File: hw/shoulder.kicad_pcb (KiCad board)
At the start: 2 copper layers, 60 x 40 mm, 27 parts, among them J1 IDC_02X07, U1 OSRB38C9BA, U2 OSRB38C9BA, U3 OSRB38C9BA, U4 OSRB38C9BA, U5 OSRB38C9BA

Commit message: updated pcb
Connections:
- LS1 pad 3: Net-(LS1-Pad3) -> GND
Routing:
- added copper zone on B.Cu, net GND
- added copper zone on F.Cu, net GND
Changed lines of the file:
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@@
     (zones 0)
     (modules 27)
-    (nets 21)
+    (nets 20)
   )
   (page A4)
@@
   (setup
     (last_trace_width 0.25)
+    (user_trace_width 0.5)
+    (user_trace_width 1)
     (trace_clearance 0.2)
     (zone_clearance 0.508)
@@
     (mod_text_size 1 1)
     (mod_text_width 0.15)
-    (pad_size 1.524 1.524)
-    (pad_drill 0.762)
+    (pad_size 6 3)
+    (pad_drill 2)
     (pad_to_mask_clearance 0.2)
     (aux_axis_origin 0 0)
@@
   (net 18 /SP+)
   (net 19 /SP-)
-  (net 20 "Net-(LS1-Pad3)")
   (net_class Default "Toto je výchozí třída sítě."
     (clearance 0.2)
@@
     (add_net "Net-(D2-Pad2)")
     (add_net "Net-(D2-Pad3)")
-    (add_net "Net-(LS1-Pad3)")
   )
   (module KLIB_Audio:REP-ABS-224-RC (layer F.Cu)
@@
     (fp_line (start 10 -20) (end 10 -19.75) (layer F.SilkS) (width 0.15))
     (fp_line (start -10 -20) (end -10 -19.75) (layer F.SilkS) (width 0.15))
-    (pad 1 smd rect (at -3 21 90) (size 4 3) (layers B.Cu B.Paste B.Mask)
+    (pad 1 smd rect (at 24 13 90) (size 1.5 3) (layers B.Cu B.Paste B.Mask)
       (net 18 /SP+))
-    (pad 2 smd rect (at 3 21 90) (size 4 3) (layers B.Cu B.Paste B.Mask)
+    (pad 2 smd oval (at 24 18 90) (size 1.5 3) (layers B.Cu B.Paste B.Mask)
       (net 19 /SP-))
     (pad 3 thru_hole oval (at 8 18 90) (size 6 3) (drill 2 (offset 1 0)) (layers *.Cu *.Mask)
-      (net 20 "Net-(LS1-Pad3)"))
+      (net 17 GND) (zone_connect 2))
     (pad 3 thru_hole oval (at 8 -18 90) (size 6 3) (drill 2 (offset 1 0)) (layers *.Cu *.Mask)
-      (net 20 "Net-(LS1-Pad3)"))
+      (net 17 GND) (zone_connect 2))
     (pad 3 thru_hole oval (at -8 -18 90) (size 6 3) (drill 2 (offset -1 0)) (layers *.Cu *.Mask)
-      (net 20 "Net-(LS1-Pad3)"))
+      (net 17 GND) (zone_connect 2))
     (pad 3 thru_hole oval (at -8 18 90) (size 6 3) (drill 2 (offset -1 0)) (layers *.Cu *.Mask)
-      (net 20 "Net-(LS1-Pad3)"))
+      (net 17 GND) (zone_connect 2))
     (pad 3 thru_hole oval (at 11 -18 90) (size 6 3) (drill 2 (offset -1 0)) (layers *.Cu *.Mask)
-      (net 20 "Net-(LS1-Pad3)"))
+      (net 17 GND) (zone_connect 2))
     (pad 3 thru_hole oval (at -11 -18 90) (size 6 3) (drill 2 (offset 1 0)) (layers *.Cu *.Mask)
-      (net 20 "Net-(LS1-Pad3)"))
+      (net 17 GND) (zone_connect 2))
     (pad 3 thru_hole oval (at 11 18 90) (size 6 3) (drill 2 (offset -1 0)) (layers *.Cu *.Mask)
-      (net 20 "Net-(LS1-Pad3)"))
+      (net 17 GND) (zone_connect 2))
     (pad 3 thru_hole oval (at -11 18 90) (size 6 3) (drill 2 (offset 1 0)) (layers *.Cu *.Mask)
-      (net 20 "Net-(LS1-Pad3)"))
+      (net 17 GND) (zone_connect 2))
     (model "$(KIPRJMOD)/project.3dshapes/ABS-224-RC.wrl"
       (at (xyz 0 0 0))
@@
   (gr_line (start 185 120) (end 185 80) (layer Edge.Cuts) (width 0.15))
   (gr_line (start 125 120) (end 185 120) (layer Edge.Cuts) (width 0.15))
+  (zone (net 17) (net_name GND) (layer F.Cu) (hatch edge 0.508)
+    (connect_pads (clearance 0.508))
+    (min_thickness 0.254)
+    (fill yes (arc_segments 16) (thermal_gap 0.508) (thermal_bridge_width 0.508))
+    (polygon
+      (pts
+        (xy 125 120) (xy 185 120) (xy 185 80) (xy 125 80)
+      )
+    )
+  )
+  (zone (net 17) (net_name GND) (layer B.Cu) (hatch edge 0.508)
+    (connect_pads (clearance 0.508))
+    (min_thickness 0.254)
+    (fill yes (arc_segments 16) (thermal_gap 0.508) (thermal_bridge_width 0.508))
+    (polygon
+      (pts
+        (xy 125 80) (xy 185 80) (xy 185 120) (xy 125 120)
+      )
+    )
+  )
 )

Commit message: updated pcb
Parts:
- moved C1 0.50 mm to (136.5, 83.5)
- moved C2 0.50 mm to (173.5, 83.5)
- moved R1 0.50 mm to (136.5, 86.2)
- moved R10 0.50 mm to (173.5, 90.2)
- moved R11 0.50 mm to (173.5, 88.2)
- moved R2 0.50 mm to (173.5, 86.2)
- moved R6 0.50 mm to (136.5, 88.2)
- moved R7 0.50 mm to (136.5, 90.2)
- moved R8 0.50 mm to (136.5, 92.2)
- moved R9 0.50 mm to (173.5, 92.2)
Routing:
- net +5V: track 0.00 -> 121.1 mm, vias 0 -> 8
- net /IR_RX: track 0.00 -> 67.0 mm
- net /SP-: track 0.00 -> 14.4 mm
- net Net-(C4-Pad1): track 0.00 -> 11.7 mm
- net Net-(C3-Pad1): track 0.00 -> 8.34 mm
- net /SP+: track 0.00 -> 6.00 mm
- net Net-(C5-Pad1): track 0.00 -> 5.78 mm
- net Net-(D2-Pad3): track 0.00 -> 4.03 mm
- net Net-(D1-Pad1): track 0.00 -> 4.03 mm
- net Net-(D2-Pad2): track 0.00 -> 3.90 mm
- net Net-(D1-Pad2): track 0.00 -> 3.90 mm
- net Net-(D2-Pad1): track 0.00 -> 3.78 mm
- net Net-(D1-Pad3): track 0.00 -> 3.78 mm

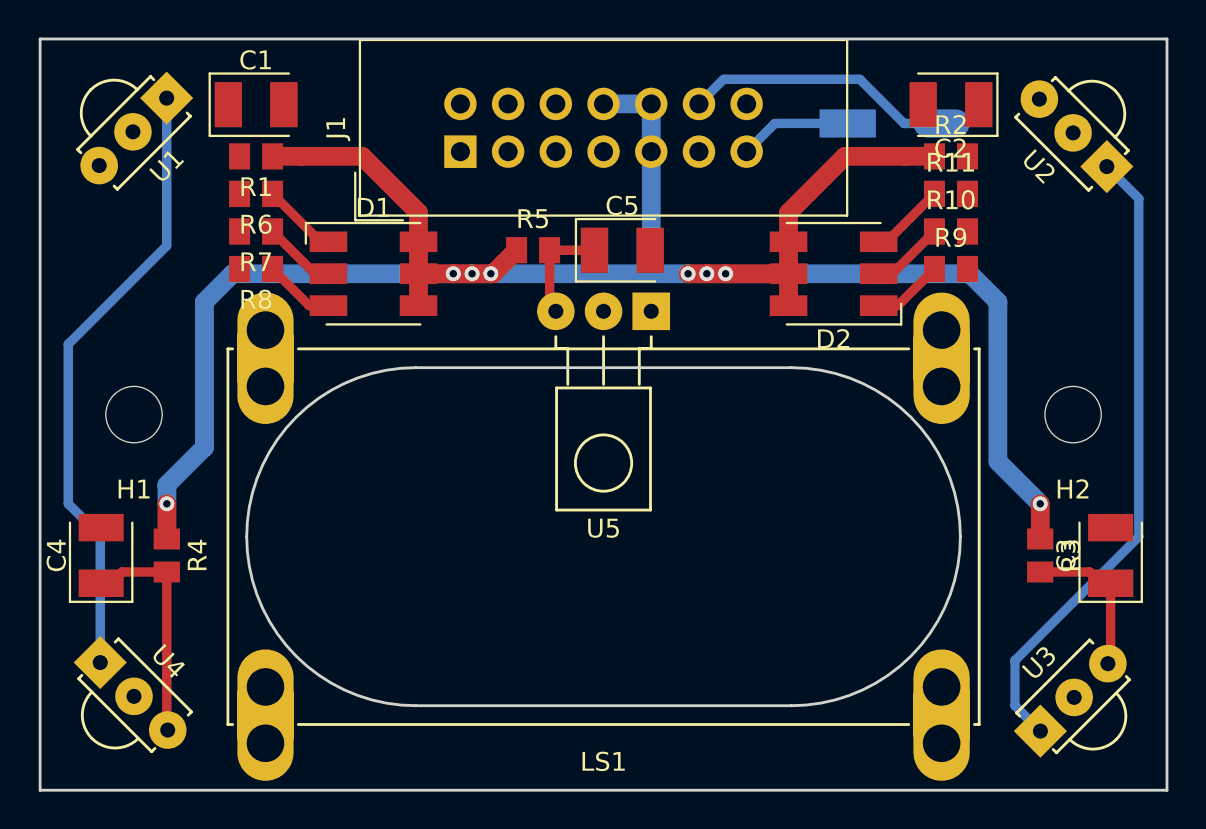
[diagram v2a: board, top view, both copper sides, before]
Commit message: updated pcb all nets conected
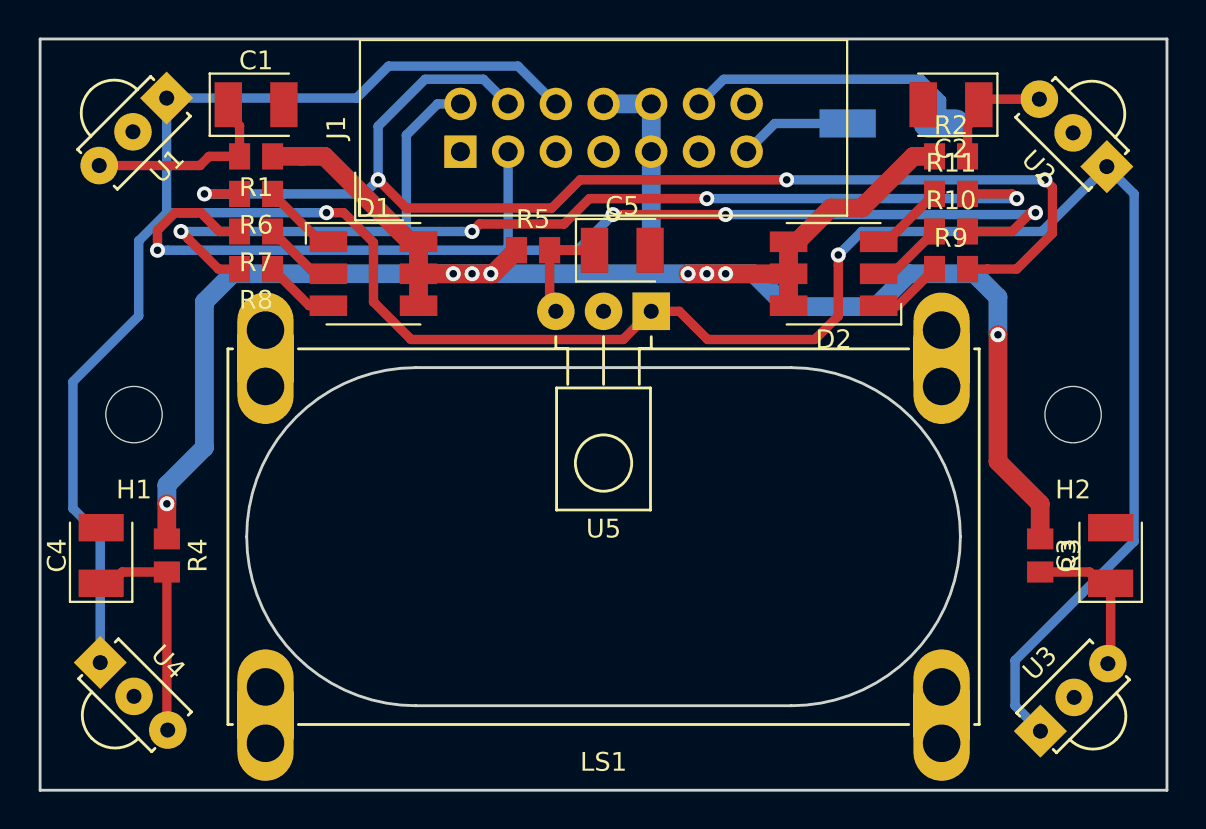
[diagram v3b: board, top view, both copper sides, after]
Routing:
- net /IR_RX: track 67.0 -> 150.5 mm, vias 0 -> 2
- net /PWM_B: track 0.00 -> 67.8 mm, vias 0 -> 4
- net /PWM_G: track 0.00 -> 63.2 mm, vias 0 -> 4
- net /PWM_R: track 0.00 -> 60.6 mm, vias 0 -> 4
- net Net-(C1-Pad1): track 0.00 -> 10.7 mm
- net Net-(C2-Pad1): track 0.00 -> 6.36 mm
- net /SP-: track 14.4 -> 15.2 mm

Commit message: updated pcb
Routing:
- net /IR_RX: track 150.5 -> 156.3 mm, vias 2 -> 3
- net +5V: track 120.9 -> 119.4 mm
- net /PWM_B: track 67.8 -> 66.8 mm
- net /PWM_R: track 60.6 -> 59.9 mm

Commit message: updated pcb
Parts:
- added G***: LOGO, KLIB_Logo:wykys_small_skill, F.Cu at (130.5, 94.8)
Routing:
- net GND: vias 0 -> 6
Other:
- board text added: "SHOULDER V3"

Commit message: updated pcb
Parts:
- added REF**: Fiducial_Pad_1mm_Outer_2mm, KLIB_Mechanical:Fiducial_Pad_1mm_Outer_2mm, F.Cu at (180.0, 93.0)
- added REF**: Fiducial_Pad_1mm_Outer_2mm, KLIB_Mechanical:Fiducial_Pad_1mm_Outer_2mm, F.Cu at (128.0, 91.0)
- added REF**: Fiducial_Pad_1mm_Outer_2mm, KLIB_Mechanical:Fiducial_Pad_1mm_Outer_2mm, F.Cu at (177.0, 112.0)
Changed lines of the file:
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@@
     (tracks 217)
     (zones 0)
-    (modules 28)
+    (modules 31)
     (nets 20)
   )
@@
     (fp_line (start 9 10) (end 9 -10) (layer F.Fab) (width 0.15))
     (fp_arc (start 0 -10) (end 0 -19) (angle 90) (layer F.Fab) (width 0.15))
-    (fp_text user %R (at 2 0 180) (layer F.Fab)
+    (fp_text user %R (at -1.5 0 180) (layer F.Fab)
       (effects (font (size 1 1) (thickness 0.15)))
     )
@@
       (xy 0.058362 -0.86999)) (layer F.SilkS) (width 0.01))
   )
+  (module KLIB_Mechanical:Fiducial_Pad_1mm_Outer_2mm (layer F.Cu)
+    (at 180 93)
+    (descr "Circular Fiducial, 0.5mm bare copper top; 1mm keepout (Level C)")
+    (tags marker)
+    (attr virtual)
+    (fp_text reference REF** (at 0 -1.5) (layer F.SilkS) hide
+      (effects (font (size 1 1) (thickness 0.15)))
+    )
+    (fp_text value Fiducial_Pad_1mm_Outer_2mm (at 0 1.5) (layer F.Fab)
+      (effects (font (size 1 1) (thickness 0.15)))
+    )
+    (fp_circle (center 0 0) (end 0.75 0) (layer F.CrtYd) (width 0.05))
+    (fp_text user %R (at 0 0) (layer F.Fab)
+      (effects (font (size 0.2 0.2) (thickness 0.04)))
+    )
+    (fp_circle (center 0 0) (end 0.5 0) (layer F.Fab) (width 0.1))
+    (pad ~ smd circle (at 0 0) (size 1 1) (layers F.Cu F.Mask)
+      (solder_mask_margin 0.5) (clearance 0.5))
+  )
+  (module KLIB_Mechanical:Fiducial_Pad_1mm_Outer_2mm (layer F.Cu)
+    (at 128 91)
+    (descr "Circular Fiducial, 0.5mm bare copper top; 1mm keepout (Level C)")
+    (tags marker)
+    (attr virtual)
+    (fp_text reference REF** (at 0 -1.5) (layer F.SilkS) hide
+      (effects (font (size 1 1) (thickness 0.15)))
+    )
+    (fp_text value Fiducial_Pad_1mm_Outer_2mm (at 0 1.5) (layer F.Fab)
+      (effects (font (size 1 1) (thickness 0.15)))
+    )
+    (fp_circle (center 0 0) (end 0.75 0) (layer F.CrtYd) (width 0.05))
+    (fp_text user %R (at 0 0) (layer F.Fab)
+      (effects (font (size 0.2 0.2) (thickness 0.04)))
+    )
+    (fp_circle (center 0 0) (end 0.5 0) (layer F.Fab) (width 0.1))
+    (pad ~ smd circle (at 0 0) (size 1 1) (layers F.Cu F.Mask)
+      (solder_mask_margin 0.5) (clearance 0.5))
+  )
+  (module KLIB_Mechanical:Fiducial_Pad_1mm_Outer_2mm (layer F.Cu)
+    (at 177 112)
+    (descr "Circular Fiducial, 0.5mm bare copper top; 1mm keepout (Level C)")
+    (tags marker)
+    (attr virtual)
+    (fp_text reference REF** (at 0 -1.5) (layer F.SilkS) hide
+      (effects (font (size 1 1) (thickness 0.15)))
+    )
+    (fp_text value Fiducial_Pad_1mm_Outer_2mm (at 0 1.5) (layer F.Fab)
+      (effects (font (size 1 1) (thickness 0.15)))
+    )
+    (fp_circle (center 0 0) (end 0.75 0) (layer F.CrtYd) (width 0.05))
+    (fp_text user %R (at 0 0) (layer F.Fab)
+      (effects (font (size 0.2 0.2) (thickness 0.04)))
+    )
+    (fp_circle (center 0 0) (end 0.5 0) (layer F.Fab) (width 0.1))
+    (pad ~ smd circle (at 0 0) (size 1 1) (layers F.Cu F.Mask)
+      (solder_mask_margin 0.5) (clearance 0.5))
+  )
   (gr_text "SHOULDER V3" (at 155 118.25) (layer F.SilkS)
